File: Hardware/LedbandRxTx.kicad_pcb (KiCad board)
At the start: 2 copper layers, 117 x 60 mm, 74 parts, among them Q1 LED_RGB 5050, SW1 BUTTON, SW2 BUTTON, SW3 BUTTON, SW4 BUTTON, SW5 SWITCH, SW6 DIPx4

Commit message: PCB routing started. Antenna under construction
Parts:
- C10, C13, C15, C17, C19, C21, C22, C7, C8, DD1, DD2, F1, F2, F3, F4, L2, Q1, R3, R4, R5, R7, R8, RP1, RP2, SW1, SW2, SW3, SW4, SW6, TP1, TP2, TP3: moved to B.Cu
- SW5: value SWITCH -> SWITCH_H
- moved RP1 131.0 mm to (84.0, 63.0)
- moved F1 105.2 mm to (103.0, 114.5), turned to 180 degrees
- moved SW6 99.8 mm to (103.2, 110.8), turned to 90 degrees
- moved F2 97.3 mm to (103.0, 112.0), turned to 180 degrees
- moved F4 96.2 mm to (103.0, 107.0), turned to 180 degrees
- moved R3 92.8 mm to (132.8, 67.0), turned to 180 degrees
- moved R4 92.2 mm to (132.8, 65.2), turned to 180 degrees
- moved R5 90.8 mm to (132.8, 68.8), turned to 180 degrees
- moved F3 90.2 mm to (103.0, 109.5), turned to 180 degrees
- moved C17 87.2 mm to (117.8, 102.8), turned to 180 degrees
- moved C15 80.4 mm to (127.0, 109.0), turned to 270 degrees
- moved C21 75.4 mm to (127.8, 93.0), turned to 90 degrees
- moved C13 74.1 mm to (117.2, 100.8), turned to 180 degrees
- moved C19 73.9 mm to (124.5, 93.0), turned to 90 degrees
- moved L2 72.9 mm to (115.8, 95.8), turned to 180 degrees
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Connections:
- SW5 pad H: (no net) -> GND
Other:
- net class Default: via_dia 0.9 -> 0.8; via_drill 0.4 -> 0.3
- net class WideWide added: clearance 0.3, trace_width 2, via_dia 1.2, via_drill 0.6

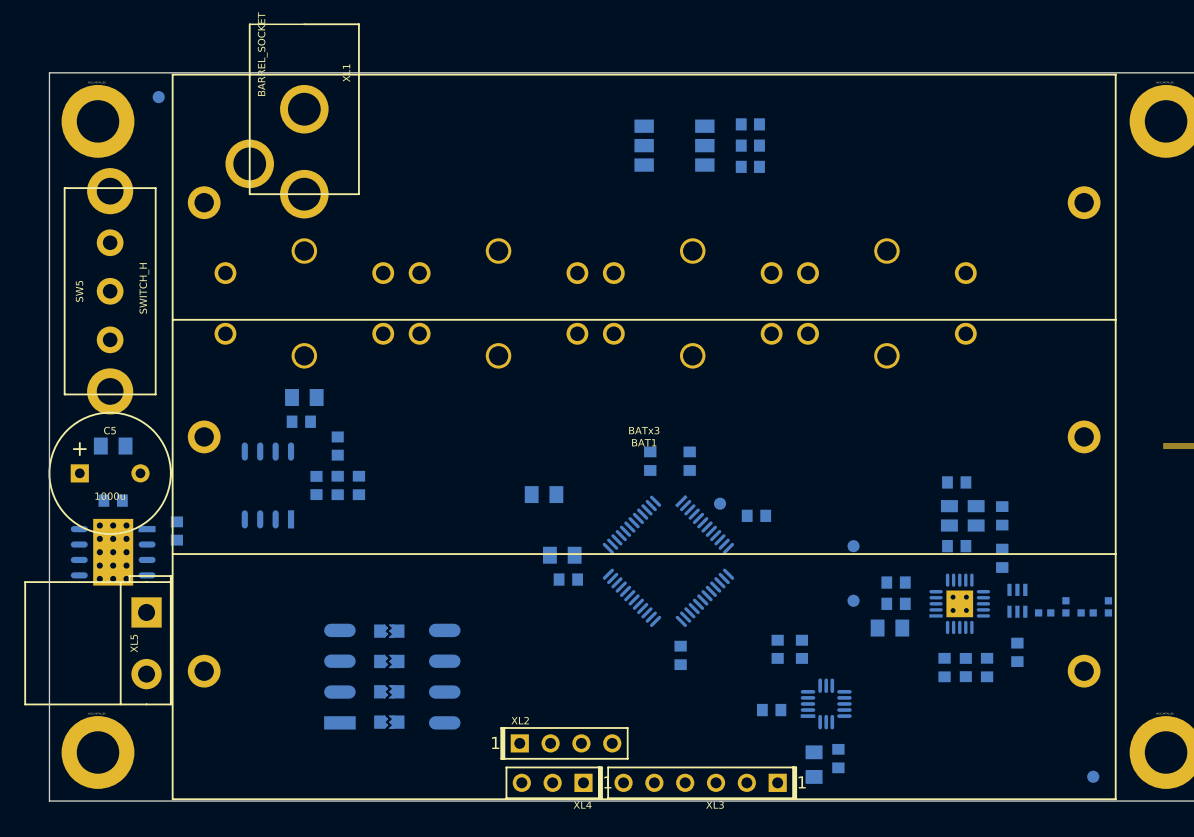
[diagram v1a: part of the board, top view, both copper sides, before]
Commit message: PCB routed, antenna still in progress
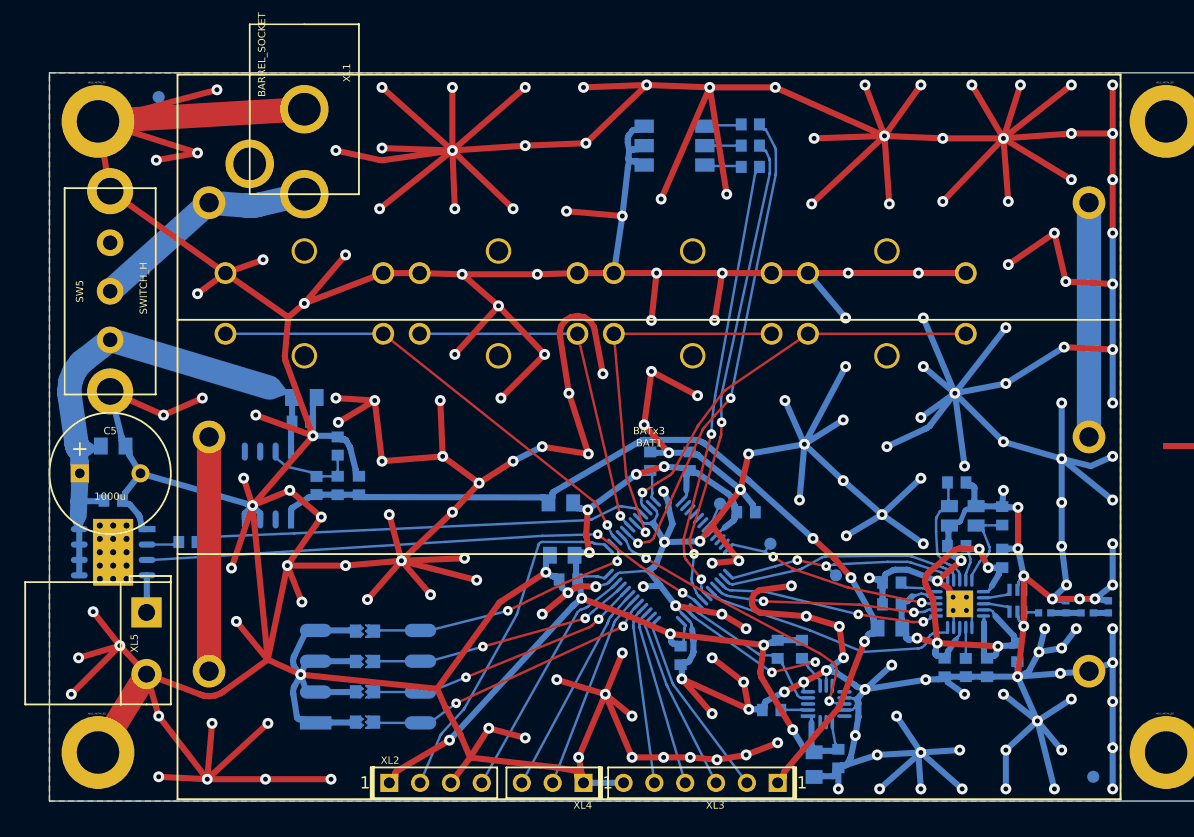
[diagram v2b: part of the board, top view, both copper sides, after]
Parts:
- moved XL2 11.2 mm to (103.0, 119.5)
- moved TP3 8.31 mm to (134.4, 99.8)
- moved TP2 2.80 mm to (139.8, 102.4)
- moved F1 2.00 mm to (101.0, 114.5)
- moved F2 2.00 mm to (101.0, 112.0)
- moved F3 2.00 mm to (101.0, 109.5)
- moved F4 2.00 mm to (101.0, 107.0)
- moved SW6 2.00 mm to (101.2, 110.8)
- moved L2 1.54 mm to (117.1, 96.4)
- moved R9 1.28 mm to (86.4, 99.7), turned to 180 degrees
- moved C22 0.90 mm to (132.4, 97.2)
- moved BAT1 0.40 mm to (124.4, 91.0)
- moved C20 0.35 mm to (144.4, 104.8)
- moved C11 0.35 mm to (144.4, 103.0)
- turned SW1 to 180 degrees
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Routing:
- net GND: track 0.00 -> 1268.1 mm, vias 0 -> 223
- net /PWR_MCU: track 0.00 -> 102.2 mm, vias 0 -> 9
- net +3.3V: track 0.00 -> 74.1 mm, vias 0 -> 3
- net /PWR_CC: track 0.00 -> 53.6 mm, vias 0 -> 5
- net +BATT: track 0.00 -> 51.4 mm
- net /Ch1_ERROR: track 0.00 -> 47.3 mm, vias 0 -> 2
- net /GREEN_LED: track 0.00 -> 39.5 mm, vias 0 -> 2
- net /RED_LED: track 0.00 -> 39.0 mm, vias 0 -> 2
- net /Btn1: track 0.00 -> 38.9 mm, vias 0 -> 1
- net /Ch1_IN: track 0.00 -> 37.4 mm
- net /BLUE_LED: track 0.00 -> 36.7 mm, vias 0 -> 2
- net /Btn4: track 0.00 -> 33.9 mm, vias 0 -> 1
- net /Btn3: track 0.00 -> 30.9 mm, vias 0 -> 1
- net /Btn2: track 0.00 -> 29.6 mm, vias 0 -> 1
- net /SWCLK: track 0.00 -> 28.1 mm
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- added copper zone on B.Cu, net GND
- added copper zone on F.Cu, net GND

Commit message: + PCB is ready, sent to production
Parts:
- added R10: 100k, Resistors:RES_0603, B.Cu at (104.4, 89.6)
- added R11: 100k, Resistors:RES_0603, B.Cu at (104.4, 92.8)
- ANT1: footprint Radio:ANT_868_MEANDER_SALEM -> Radio:ANT_INVF_LEDBANDRXTX; moved to B.Cu
- XL5: value CONN_2 -> CONN_3; footprint Connectors:TermiBlockHeader_508_x2_R -> Connectors:TermiBlockHeader_508_x3_R
- moved DA2 3.71 mm to (80.0, 96.8)
- moved ANT1 3.51 mm to (163.2, 91.5), turned to 0 degrees
- moved R9 3.48 mm to (86.0, 96.2)
- moved C25 3.45 mm to (80.2, 92.8)
- moved C27 2.27 mm to (78.8, 90.0)
- moved SW5 2.13 mm to (81.6, 77.6)
- moved C5 1.22 mm to (80.2, 92.8)
- moved XL5 0.72 mm to (83.4, 108.6)
- moved RP2 0.25 mm to (160.8, 119.0)
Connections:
- DD1 pad 10: (no net) -> /DataIn
- DD1 pad 11: (no net) -> /BatMeas
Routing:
- net /DataIn: track 0.00 -> 53.1 mm, vias 0 -> 2
- net /BatMeas: track 0.00 -> 40.0 mm
- net GND: track 1268.1 -> 1303.7 mm, vias 223 -> 243
- net /ANT2: track 1.25 -> 14.0 mm
- net +BATT: track 51.4 -> 54.9 mm
- net /BAT_IN: track 18.9 -> 16.8 mm
- net /Ch1_ERROR: track 47.3 -> 48.5 mm
- net /Ch1_IN: track 37.4 -> 38.4 mm
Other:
- board size 117 x 60 mm -> 112.2 x 60 mm
- board text added: "Acc"
- board text added: "Power"
- board text added: "PwrSw"
- board text added: "Radio"
- board text added: "SWD"
- board text added: "UART"
